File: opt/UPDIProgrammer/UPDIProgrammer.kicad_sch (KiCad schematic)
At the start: 21 parts, among them J2 USB_C_Receptacle_USB2.0_14P, U1 CH340N, U2 ATtiny1616-M

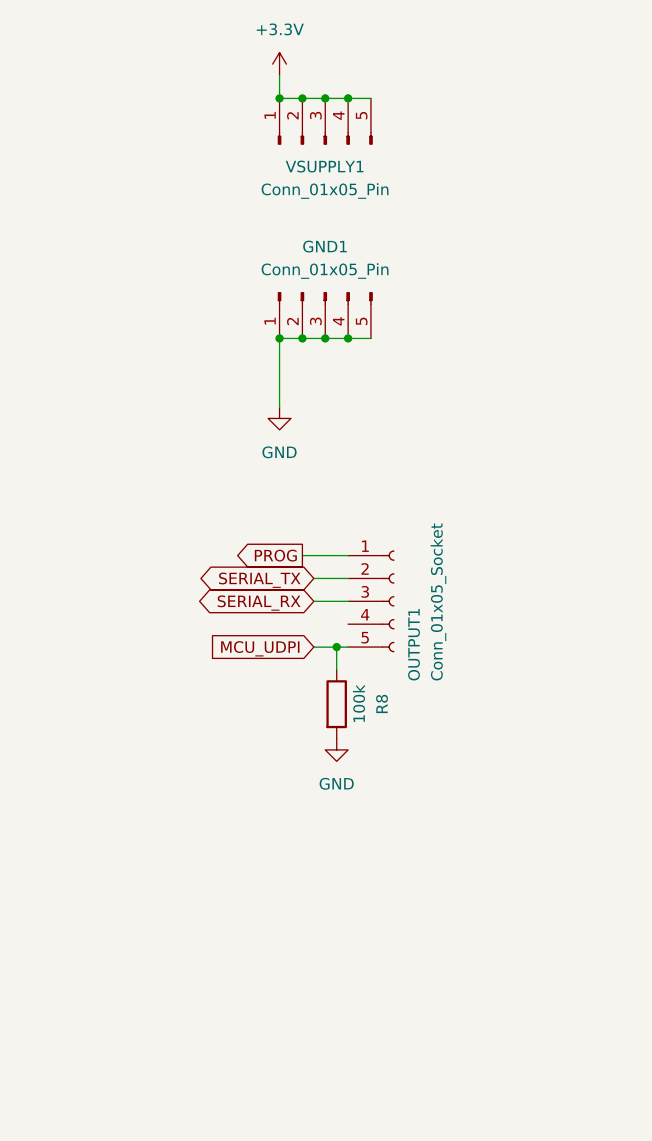
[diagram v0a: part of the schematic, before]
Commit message: Update the UPDI Programmer.
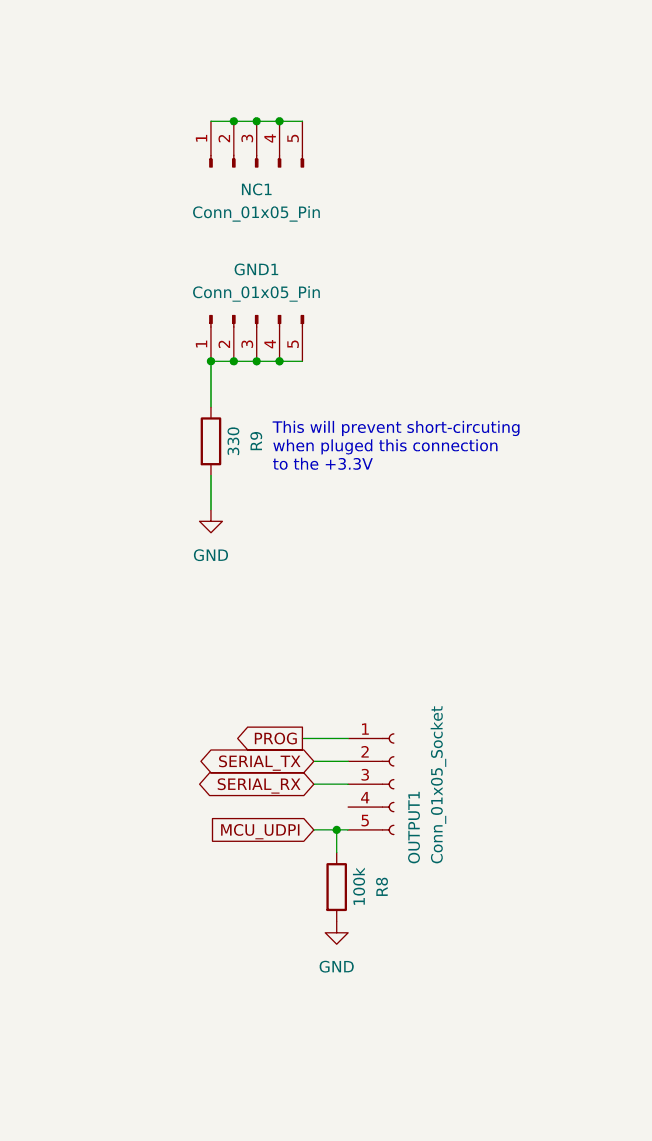
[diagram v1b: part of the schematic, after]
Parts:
- added R9: 330, Resistor_SMD:R_0402_1005Metric, symbol Device:R
- renumbered VSUPPLY1 to NC1
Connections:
- net GND: now also R9.2; no longer GND1.1 (Pin_1), GND1.2 (Pin_2), GND1.3 (Pin_3), GND1.4 (Pin_4), GND1.5 (Pin_5)
- net +3.3V: no longer names the net of NC1.1 (Pin_1), NC1.2 (Pin_2), NC1.3 (Pin_3), NC1.4 (Pin_4), NC1.5 (Pin_5)
- new net: GND1.1 (Pin_1), GND1.2 (Pin_2), GND1.3 (Pin_3), GND1.4 (Pin_4), GND1.5 (Pin_5), R9.1
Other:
- note added: "This will prevent short-circuting when pluged this connection to the +3.3V"
- moved on the sheet: GND1, NC1, OUTPUT1, R8
